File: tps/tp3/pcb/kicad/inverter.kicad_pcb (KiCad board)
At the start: 2 copper layers, 28 parts, among them Q1 IRF820, Q2 IRF820, Q3 IRF820, Q4 IRF820, Q5 IRF820, Q6 IRF820, U1 IR2110-A, U2 ESP32-DEVKIT-V1, U3 IR2110-B, U4 IR2110-C

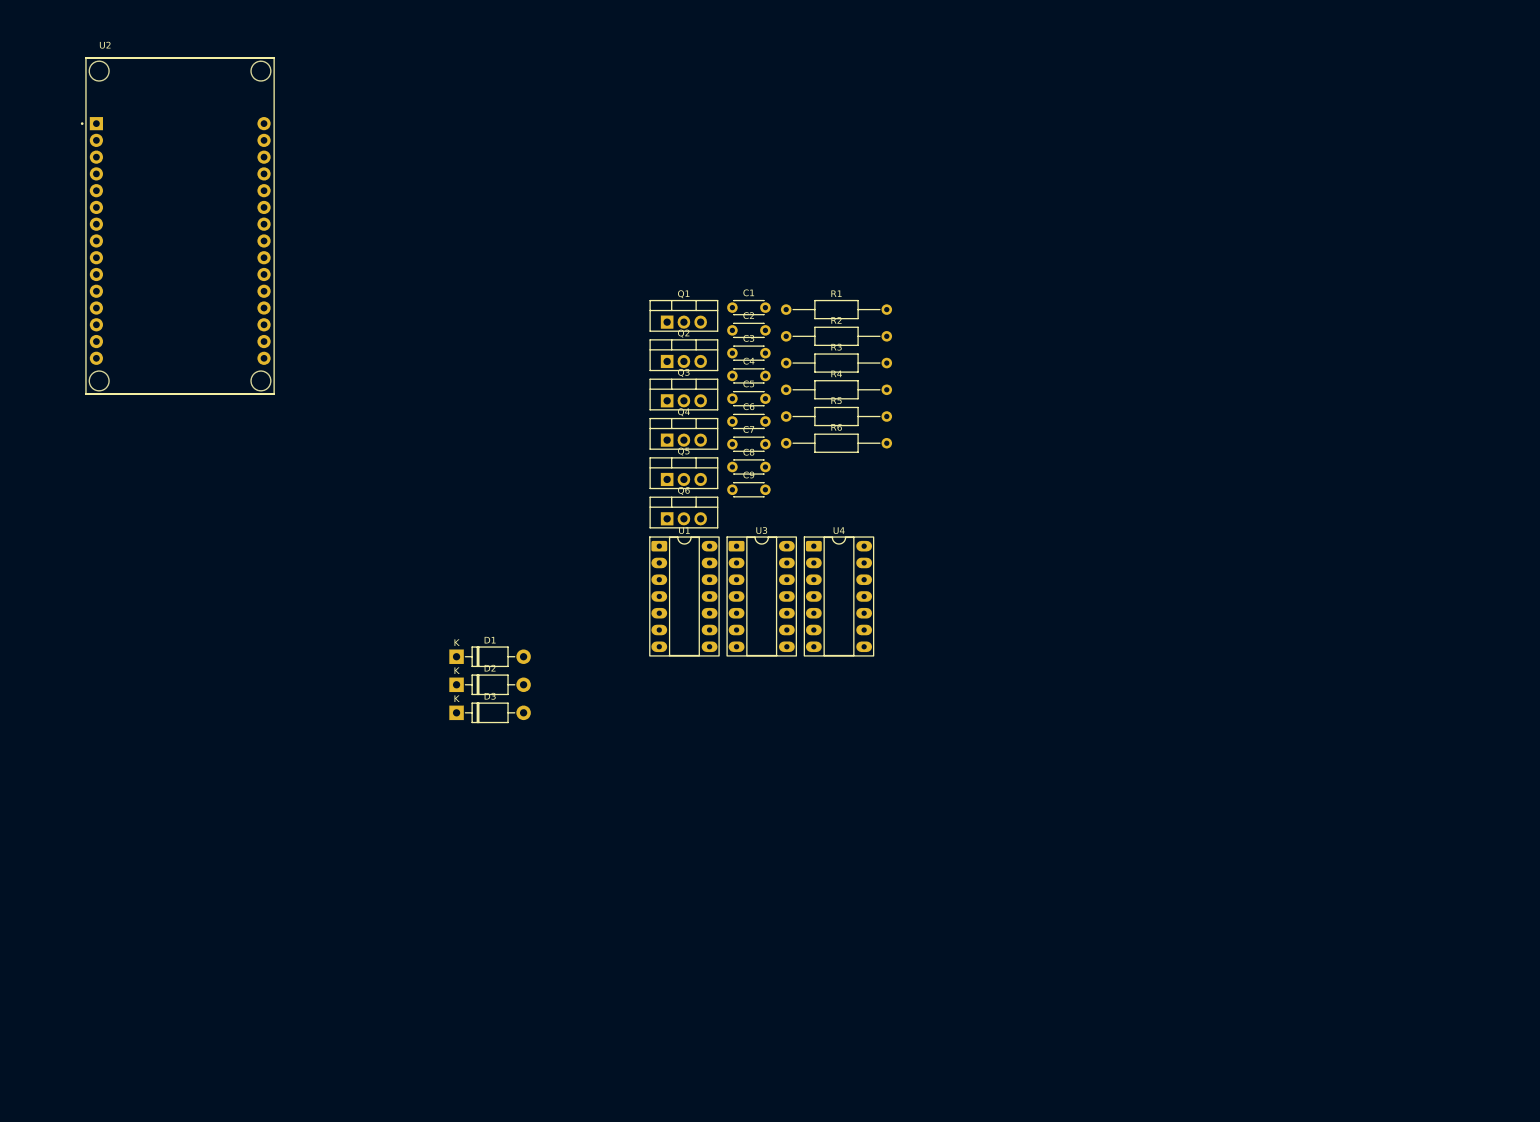
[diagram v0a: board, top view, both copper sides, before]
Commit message: fix inverter sch after feedback and real component sizes, start PCB routing
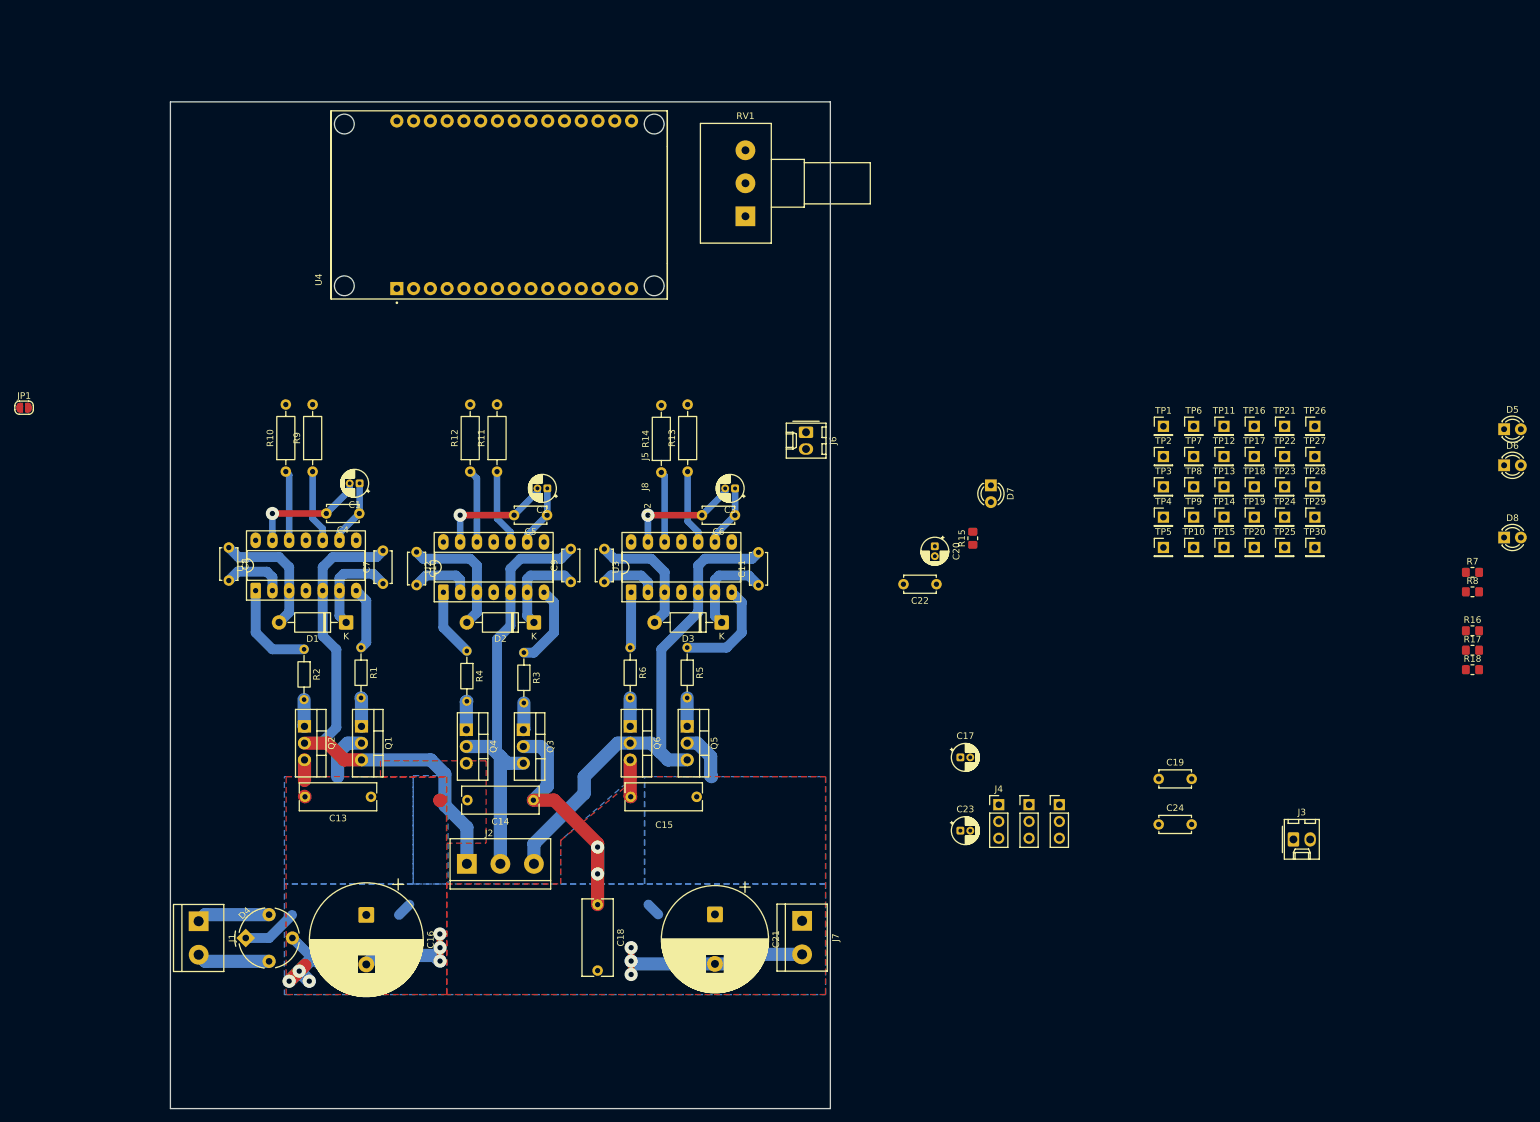
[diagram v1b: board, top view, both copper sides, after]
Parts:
- added C10: 1u-50V, Capacitor_THT:C_Disc_D4.7mm_W2.5mm_P5.00mm, F.Cu at (93.5, 87.4)
- added C11: 1u-50V, Capacitor_THT:C_Disc_D4.7mm_W2.5mm_P5.00mm, F.Cu at (145.3, 92.4)
- added C12: 1u-50V, Capacitor_THT:C_Disc_D4.7mm_W2.5mm_P5.00mm, F.Cu at (121.9, 86.9)
- added C13: 22n-400V, Capacitor_THT:C_Rect_L11.5mm_W4.0mm_P10.00mm_MKT, F.Cu at (86.6, 124.5)
- added C14: 22n-400V, Capacitor_THT:C_Rect_L11.5mm_W4.0mm_P10.00mm_MKT, F.Cu at (111.2, 125.0)
- added C15: 22n-400V, Capacitor_THT:C_Rect_L11.5mm_W4.0mm_P10.00mm_MKT, F.Cu at (135.9, 124.5)
- added C16: 100u-450V, Capacitor_THT:CP_Radial_D17.0mm_P7.50mm, F.Cu at (85.9, 142.4)
- added C17: 10u-25V, Capacitor_THT:CP_Radial_D4.0mm_P1.50mm, F.Cu at (175.9, 118.5)
- added C18: 10n-400V, Capacitor_THT:C_Rect_L11.5mm_W4.5mm_P10.00mm_MKT, F.Cu at (120.9, 140.8)
- added C19: 1u-50V, Capacitor_THT:C_Disc_D4.7mm_W2.5mm_P5.00mm, F.Cu at (205.9, 121.8)
- added C20: 10u-25V, Capacitor_THT:CP_Radial_D4.0mm_P1.50mm, F.Cu at (172.0, 86.5)
- added C21: 47u-450V, Capacitor_THT:CP_Radial_D16.0mm_P7.50mm, F.Cu at (138.7, 142.3)
- added C22: 1u-50V, Capacitor_THT:C_Disc_D4.7mm_W2.5mm_P5.00mm, F.Cu at (172.2, 92.2)
- added C23: 10u-25V, Capacitor_THT:CP_Radial_D4.0mm_P1.50mm, F.Cu at (175.9, 129.6)
- added C24: 1u-50V, Capacitor_THT:C_Disc_D4.7mm_W2.5mm_P5.00mm, F.Cu at (205.9, 128.7)
- added D4: W10M, Diode_THT:Diode_Bridge_Round_D9.0mm, F.Cu at (67.6, 145.9)
- added D5: Red, LED_THT:LED_D3.0mm, F.Cu at (258.3, 68.8)
- added D6: Red, LED_THT:LED_D3.0mm, F.Cu at (258.3, 74.2)
- added D7: Red, LED_THT:LED_D3.0mm, F.Cu at (180.5, 77.3)
- added D8: Red, LED_THT:LED_D3.0mm, F.Cu at (258.3, 85.2)
- added J1: 220Vac In, TerminalBlock:TerminalBlock_bornier-2_P5.08mm, F.Cu at (60.5, 143.3)
- added J2: Motor, TerminalBlock:TerminalBlock_bornier-3_P5.08mm, F.Cu at (101.1, 134.6)
- added J3: 5Vext In, Connector_Molex:Molex_KK-254_AE-6410-02A_1x02_P2.54mm_Vertical, F.Cu at (226.3, 130.9)
- added J4: Conn_01x03_Pin, Connector_PinHeader_2.54mm:PinHeader_1x03_P2.54mm_Vertical, F.Cu at (181.7, 125.7)
- added J5: Conn_01x03_Pin, Connector_PinHeader_2.54mm:PinHeader_1x03_P2.54mm_Vertical, F.Cu at (186.3, 125.7)
- added J6: 15Vext In, Connector_Molex:Molex_KK-254_AE-6410-02A_1x02_P2.54mm_Vertical, F.Cu at (152.5, 69.2)
- added J7: Vd out, TerminalBlock:TerminalBlock_bornier-2_P5.08mm, F.Cu at (151.9, 143.3)
- added J8: Conn_01x03_Pin, Connector_PinHeader_2.54mm:PinHeader_1x03_P2.54mm_Vertical, F.Cu at (190.9, 125.7)
- added JP1: Jumper_2_Bridged, Jumper:SolderJumper-2_P1.3mm_Open_RoundedPad1.0x1.5mm, F.Cu at (34.0, 65.5)
- added R10: 10, Resistor_THT:R_Axial_DIN0207_L6.3mm_D2.5mm_P10.16mm_Horizontal, F.Cu at (73.7, 75.2)
- added R11: 10, Resistor_THT:R_Axial_DIN0207_L6.3mm_D2.5mm_P10.16mm_Horizontal, F.Cu at (105.7, 75.2)
- added R12: 10, Resistor_THT:R_Axial_DIN0207_L6.3mm_D2.5mm_P10.16mm_Horizontal, F.Cu at (101.6, 75.2)
- added R13: 10, Resistor_THT:R_Axial_DIN0207_L6.3mm_D2.5mm_P10.16mm_Horizontal, F.Cu at (134.5, 75.2)
- added R14: 10, Resistor_THT:R_Axial_DIN0207_L6.3mm_D2.5mm_P10.16mm_Horizontal, F.Cu at (130.6, 75.3)
- added R15: 2.7k, Resistor_SMD:R_0805_2012Metric_Pad1.20x1.40mm_HandSolder, F.Cu at (177.8, 85.3)
- added R16: 150k, Resistor_SMD:R_0805_2012Metric_Pad1.20x1.40mm_HandSolder, F.Cu at (253.5, 99.3)
- added R17: 150k, Resistor_SMD:R_0805_2012Metric_Pad1.20x1.40mm_HandSolder, F.Cu at (253.5, 102.2)
- added R18: 150k, Resistor_SMD:R_0805_2012Metric_Pad1.20x1.40mm_HandSolder, F.Cu at (253.5, 105.2)
- added R7: 560, Resistor_SMD:R_0805_2012Metric_Pad1.20x1.40mm_HandSolder, F.Cu at (253.5, 90.5)
- added R8: 220, Resistor_SMD:R_0805_2012Metric_Pad1.20x1.40mm_HandSolder, F.Cu at (253.5, 93.4)
- added R9: 10, Resistor_THT:R_Axial_DIN0207_L6.3mm_D2.5mm_P10.16mm_Horizontal, F.Cu at (77.7, 75.2)
- added RV1: 10k, Potentiometer_THT:Potentiometer_Alps_RK163_Single_Horizontal, F.Cu at (143.3, 36.5)
- added TP1: TestPoint, Connector_PinHeader_2.54mm:PinHeader_1x01_P2.54mm_Vertical, F.Cu at (206.6, 68.3)
- added TP10: TestPoint, Connector_PinHeader_2.54mm:PinHeader_1x01_P2.54mm_Vertical, F.Cu at (211.2, 86.7)
- added TP11: TestPoint, Connector_PinHeader_2.54mm:PinHeader_1x01_P2.54mm_Vertical, F.Cu at (215.8, 68.3)
- added TP12: TestPoint, Connector_PinHeader_2.54mm:PinHeader_1x01_P2.54mm_Vertical, F.Cu at (215.8, 72.9)
- added TP13: TestPoint, Connector_PinHeader_2.54mm:PinHeader_1x01_P2.54mm_Vertical, F.Cu at (215.8, 77.5)
- added TP14: TestPoint, Connector_PinHeader_2.54mm:PinHeader_1x01_P2.54mm_Vertical, F.Cu at (215.8, 82.1)
- added TP15: TestPoint, Connector_PinHeader_2.54mm:PinHeader_1x01_P2.54mm_Vertical, F.Cu at (215.8, 86.7)
- added TP16: TestPoint, Connector_PinHeader_2.54mm:PinHeader_1x01_P2.54mm_Vertical, F.Cu at (220.4, 68.3)
- added TP17: TestPoint, Connector_PinHeader_2.54mm:PinHeader_1x01_P2.54mm_Vertical, F.Cu at (220.4, 72.9)
- added TP18: TestPoint, Connector_PinHeader_2.54mm:PinHeader_1x01_P2.54mm_Vertical, F.Cu at (220.4, 77.5)
- added TP19: TestPoint, Connector_PinHeader_2.54mm:PinHeader_1x01_P2.54mm_Vertical, F.Cu at (220.4, 82.1)
- added TP2: TestPoint, Connector_PinHeader_2.54mm:PinHeader_1x01_P2.54mm_Vertical, F.Cu at (206.6, 72.9)
- added TP20: TestPoint, Connector_PinHeader_2.54mm:PinHeader_1x01_P2.54mm_Vertical, F.Cu at (220.4, 86.7)
- added TP21: TestPoint, Connector_PinHeader_2.54mm:PinHeader_1x01_P2.54mm_Vertical, F.Cu at (225.0, 68.3)
- added TP22: TestPoint, Connector_PinHeader_2.54mm:PinHeader_1x01_P2.54mm_Vertical, F.Cu at (225.0, 72.9)
- added TP23: TestPoint, Connector_PinHeader_2.54mm:PinHeader_1x01_P2.54mm_Vertical, F.Cu at (225.0, 77.5)
- added TP24: TestPoint, Connector_PinHeader_2.54mm:PinHeader_1x01_P2.54mm_Vertical, F.Cu at (225.0, 82.1)
- added TP25: TestPoint, Connector_PinHeader_2.54mm:PinHeader_1x01_P2.54mm_Vertical, F.Cu at (225.0, 86.7)
- added TP26: TestPoint, Connector_PinHeader_2.54mm:PinHeader_1x01_P2.54mm_Vertical, F.Cu at (229.6, 68.3)
- added TP27: TestPoint, Connector_PinHeader_2.54mm:PinHeader_1x01_P2.54mm_Vertical, F.Cu at (229.6, 72.9)
- added TP28: TestPoint, Connector_PinHeader_2.54mm:PinHeader_1x01_P2.54mm_Vertical, F.Cu at (229.6, 77.5)
- added TP29: TestPoint, Connector_PinHeader_2.54mm:PinHeader_1x01_P2.54mm_Vertical, F.Cu at (229.6, 82.1)
- added TP3: TestPoint, Connector_PinHeader_2.54mm:PinHeader_1x01_P2.54mm_Vertical, F.Cu at (206.6, 77.5)
- added TP30: TestPoint, Connector_PinHeader_2.54mm:PinHeader_1x01_P2.54mm_Vertical, F.Cu at (229.6, 86.7)
- added TP4: TestPoint, Connector_PinHeader_2.54mm:PinHeader_1x01_P2.54mm_Vertical, F.Cu at (206.6, 82.1)
- added TP5: TestPoint, Connector_PinHeader_2.54mm:PinHeader_1x01_P2.54mm_Vertical, F.Cu at (206.6, 86.7)
- added TP6: TestPoint, Connector_PinHeader_2.54mm:PinHeader_1x01_P2.54mm_Vertical, F.Cu at (211.2, 68.3)
- added TP7: TestPoint, Connector_PinHeader_2.54mm:PinHeader_1x01_P2.54mm_Vertical, F.Cu at (211.2, 72.9)
- added TP8: TestPoint, Connector_PinHeader_2.54mm:PinHeader_1x01_P2.54mm_Vertical, F.Cu at (211.2, 77.5)
- added TP9: TestPoint, Connector_PinHeader_2.54mm:PinHeader_1x01_P2.54mm_Vertical, F.Cu at (211.2, 82.1)
- C1, C3: value 1u -> 10u-25V; footprint Capacitor_THT:C_Disc_D4.3mm_W1.9mm_P5.00mm -> Capacitor_THT:CP_Radial_D4.0mm_P1.50mm
- C2: value 10u -> 10u-25V; footprint Capacitor_THT:C_Disc_D4.3mm_W1.9mm_P5.00mm -> Capacitor_THT:CP_Radial_D4.0mm_P1.50mm
- C4, C5, C7, C8: value 1u -> 1u-50V; footprint Capacitor_THT:C_Disc_D4.3mm_W1.9mm_P5.00mm -> Capacitor_THT:C_Disc_D4.7mm_W2.5mm_P5.00mm
- C6, C9: value 10u -> 1u-50V; footprint Capacitor_THT:C_Disc_D4.3mm_W1.9mm_P5.00mm -> Capacitor_THT:C_Disc_D4.7mm_W2.5mm_P5.00mm
- D1, D2, D3: value 1N5819 -> FR104
- R1, R2, R3, R4, R5, R6: footprint Resistor_THT:R_Axial_DIN0207_L6.3mm_D2.5mm_P15.24mm_Horizontal -> Resistor_THT:R_Axial_DIN0204_L3.6mm_D1.6mm_P7.62mm_Horizontal
- U2: value ESP32-DEVKIT-V1 -> IR2110-B; footprint esp32devkitv1:MODULE_ESP32_DEVKIT_V1 -> Package_DIP:DIP-14_W7.62mm_Socket_LongPads
- U3: value IR2110-B -> IR2110-C
- U4: value IR2110-C -> ESP32-DEVKIT-V1; footprint Package_DIP:DIP-14_W7.62mm_Socket_LongPads -> esp32devkitv1:MODULE_ESP32_DEVKIT_V1
- moved R2 87.1 mm to (76.4, 102.1), turned to -90 degrees
- moved R1 82.3 mm to (85.1, 101.9), turned to -90 degrees
- moved Q2 78.0 mm to (76.5, 113.8), turned to -90 degrees
- moved C8 77.3 mm to (65.0, 86.7), turned to -90 degrees
- moved Q1 76.8 mm to (85.1, 113.8), turned to -90 degrees
- moved U4 70.4 mm to (106.0, 34.8), turned to 90 degrees
- moved U2 68.3 mm to (97.5, 93.5), turned to 90 degrees
- moved R4 62.5 mm to (101.1, 102.4), turned to -90 degrees
- moved C1 62.5 mm to (84.8, 77.0), turned to 180 degrees
- moved U1 61.5 mm to (69.1, 93.2), turned to 90 degrees
- moved C4 60.3 mm to (84.8, 81.5), turned to 180 degrees
- moved R3 59.2 mm to (109.7, 102.6), turned to -90 degrees
- moved C7 57.0 mm to (88.4, 92.2), turned to 90 degrees
- moved Q3 54.4 mm to (109.6, 114.3), turned to -90 degrees
- moved Q4 53.4 mm to (101.0, 114.3), turned to -90 degrees
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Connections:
- C1 pad 1: Net-(D1-K) -> VDD
- C1 pad 2: /OUT_A -> VSS
- C2 pad 1: VIC -> VDD
- C2 pad 2: COM -> VSS
- C5 pad 1: Net-(D2-K) -> VDD
- C5 pad 2: /OUT_B -> VSS
- C6 pad 1: VIC -> VDD
- C6 pad 2: COM -> VSS
- C7 pad 1: VDD -> Net-(D1-K)
- C7 pad 2: VSS -> /OUT_A
- C8 pad 1: Net-(D3-K) -> VDRV
- C8 pad 2: /OUT_C -> COM
- C9 pad 1: VIC -> Net-(D2-K)
- C9 pad 2: COM -> /OUT_B
- D1 pad 2: VIC -> VDRV
- D2 pad 2: VIC -> VDRV
- D3 pad 2: VIC -> VDRV
- R3 pad 1: Net-(U3-HO) -> Net-(U2-HO)
- R4 pad 1: Net-(U3-LO) -> Net-(U2-LO)
- R5 pad 1: Net-(U4-HO) -> Net-(U3-HO)
- R6 pad 1: Net-(U4-LO) -> Net-(U3-LO)
- U1 pad 3: VIC -> VDRV
- U2 pad 1: unconnected-(U2-3V3-Pad1) -> Net-(U2-LO)
- U2 pad 10: unconnected-(U2-D19-Pad10) -> /HIN_B
- U2 pad 12: unconnected-(U2-RX0-Pad12) -> /LIN_B
- U2 pad 13: unconnected-(U2-TX0-Pad13) -> VSS
- U2 pad 2: Net-(U2-GND-Pad2) -> COM
- U2 pad 3: unconnected-(U2-D15-Pad3) -> VDRV
- U2 pad 5: unconnected-(U2-D4-Pad5) -> /OUT_B
- U2 pad 6: unconnected-(U2-RX2-Pad6) -> Net-(D2-K)
- U2 pad 7: unconnected-(U2-TX2-Pad7) -> Net-(U2-HO)
- U2 pad 9: unconnected-(U2-D18-Pad9) -> VDD
- U3 pad 10: /HIN_B -> /HIN_C
- U3 pad 12: /LIN_B -> /LIN_C
- U3 pad 3: VIC -> VDRV
- U3 pad 5: /OUT_B -> /OUT_C
- U3 pad 6: Net-(D2-K) -> Net-(D3-K)
- U4 pad 1: Net-(U4-LO) -> VDD
- U4 pad 10: /HIN_C -> Net-(U4-D19)
- U4 pad 11: unconnected-(U4-SD-Pad11) -> Net-(U4-D21)
- U4 pad 12: /LIN_C -> unconnected-(U4-RX0-Pad12)
- U4 pad 13: VSS -> unconnected-(U4-TX0-Pad13)
- U4 pad 2: COM -> VSS
- U4 pad 3: VIC -> Net-(U4-D15)
- U4 pad 5: /OUT_C -> unconnected-(U4-D4-Pad5)
- U4 pad 6: Net-(D3-K) -> unconnected-(U4-RX2-Pad6)
- U4 pad 7: Net-(U4-HO) -> unconnected-(U4-TX2-Pad7)
- U4 pad 9: VDD -> Net-(U4-D18)
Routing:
- net COM: track 0.00 -> 100.2 mm, vias 0 -> 9
- net /OUT_A: track 0.00 -> 79.4 mm
- net /OUT_C: track 0.00 -> 75.7 mm
- net VD: track 0.00 -> 65.9 mm, vias 0 -> 2
- net /OUT_B: track 0.00 -> 65.8 mm
- net VDRV: track 0.00 -> 57.5 mm
- net VSS: track 0.00 -> 53.8 mm, vias 0 -> 3
- net VDD: track 0.00 -> 28.8 mm
- net Net-(U3-HO): track 0.00 -> 15.9 mm
- net Net-(U1-LO): track 0.00 -> 14.7 mm
- net Net-(D1-K): track 0.00 -> 14.6 mm
- net Net-(D3-K): track 0.00 -> 14.4 mm
- net Net-(D2-K): track 0.00 -> 14.2 mm
- net Net-(U2-HO): track 0.00 -> 12.6 mm
- net /HIN_B: track 0.00 -> 11.5 mm
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- added copper zone on F.Cu, net COM
- added copper zone on B.Cu, net VD
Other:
- board outline added: 100 x 152.5 mm

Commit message: add more 15V decoupling caps, update exported sch, add potentiometer 3D model, some routing progress
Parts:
- added C25: 10u-25V, Capacitor_THT:CP_Radial_D4.0mm_P1.50mm, F.Cu at (93.5, 82.0)
- added C26: 10u-25V, Capacitor_THT:CP_Radial_D4.0mm_P1.50mm, F.Cu at (65.0, 81.8)
- added C27: 10u-25V, Capacitor_THT:CP_Radial_D4.0mm_P1.50mm, F.Cu at (122.0, 82.0)
- R15: moved to B.Cu
- moved D7 28.8 mm to (152.0, 73.0), turned to 180 degrees
- moved R15 25.1 mm to (154.0, 77.2)
- moved C22 22.5 mm to (151.2, 84.2), turned to -90 degrees
- moved J6 9.09 mm to (151.2, 78.2)
- moved C21 1.43 mm to (137.2, 142.3)
- moved C10 0.13 mm to (93.5, 87.5)
- moved C12 0.12 mm to (122.0, 87.0)
- moved C8 0.06 mm to (65.0, 86.8)
- turned U4 to -90 degrees
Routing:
- net VDRV: track 57.5 -> 208.7 mm
- net COM: track 100.2 -> 153.1 mm
- net VD: track 65.9 -> 55.7 mm, vias 2 -> 3
- net Net-(D7-K): track 0.00 -> 4.62 mm
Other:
- board size 100 x 152.5 mm -> 100 x 150 mm

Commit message: avances pcb
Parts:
- added C28: 10u-25V, Capacitor_THT:CP_Radial_D4.0mm_P1.50mm, F.Cu at (171.0, 44.8)
- added C29: 10u-25V, Capacitor_THT:CP_Radial_D4.0mm_P1.50mm, F.Cu at (171.0, 50.3)
- added C30: 10u-25V, Capacitor_THT:CP_Radial_D4.0mm_P1.50mm, F.Cu at (171.0, 55.9)
- moved C22 47.2 mm to (190.5, 58.0)
- moved D7 47.2 mm to (191.3, 46.8)
- moved J6 47.2 mm to (190.5, 52.0)
- moved R15 47.2 mm to (193.2, 51.0)
- moved C18 31.5 mm to (89.5, 140.8)
- moved R14 23.1 mm to (144.5, 93.7)
- moved R9 22.6 mm to (64.0, 93.1)
- moved C26 21.5 mm to (62.3, 103.1), turned to -135 degrees
- moved C3 21.1 mm to (149.1, 97.5), turned to 135 degrees
- moved C8 19.9 mm to (65.9, 106.7), turned to -45 degrees
- moved D4 19.8 mm to (70.4, 126.3), turned to -45 degrees
- moved C6 19.1 mm to (146.2, 100.4), turned to 135 degrees
- moved C11 18.4 mm to (141.2, 110.4), turned to 45 degrees
- moved R10 16.7 mm to (68.0, 90.9)
- moved R13 16.2 mm to (140.2, 90.3)
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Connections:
- R10 pad 1: /LIN_A -> /HIN_A
- R10 pad 2: Net-(U4-D14) -> Net-(U4-D2)
- R11 pad 1: /HIN_B -> /LIN_B
- R11 pad 2: Net-(U4-D15) -> Net-(U4-D4)
- R12 pad 1: /LIN_B -> /HIN_B
- R12 pad 2: Net-(U4-D18) -> Net-(U4-RX2)
- R13 pad 1: /HIN_C -> /LIN_C
- R13 pad 2: Net-(U4-D19) -> Net-(U4-TX2)
- R14 pad 1: /LIN_C -> /HIN_C
- R14 pad 2: Net-(U4-D21) -> Net-(U4-D5)
- R9 pad 1: /HIN_A -> /LIN_A
- R9 pad 2: Net-(U4-D13) -> Net-(U4-D15)
- RV1 pad 2: Net-(U4-D27) -> Net-(U4-D34)
- TP29 pad 1: Net-(U4-D27) -> Net-(U4-D34)
- U4 pad 10: Net-(U4-D19) -> unconnected-(U4-D19-Pad10)
- U4 pad 11: Net-(U4-D21) -> unconnected-(U4-D21-Pad11)
- U4 pad 19: Net-(J8-Pin_1) -> Net-(U4-D34)
- U4 pad 20: Net-(J8-Pin_2) -> unconnected-(U4-D35-Pad20)
- U4 pad 22: Net-(J8-Pin_3) -> unconnected-(U4-D33-Pad22)
- U4 pad 23: unconnected-(U4-D25-Pad23) -> Net-(J8-Pin_3)
- U4 pad 24: unconnected-(U4-D26-Pad24) -> Net-(J8-Pin_2)
- U4 pad 25: Net-(U4-D27) -> Net-(J8-Pin_1)
- U4 pad 26: Net-(U4-D14) -> unconnected-(U4-D14-Pad26)
- U4 pad 28: Net-(U4-D13) -> unconnected-(U4-D13-Pad28)
- U4 pad 4: unconnected-(U4-D2-Pad4) -> Net-(U4-D2)
- U4 pad 5: unconnected-(U4-D4-Pad5) -> Net-(U4-D4)
- U4 pad 6: unconnected-(U4-RX2-Pad6) -> Net-(U4-RX2)
- U4 pad 7: unconnected-(U4-TX2-Pad7) -> Net-(U4-TX2)
- U4 pad 8: unconnected-(U4-D5-Pad8) -> Net-(U4-D5)
- U4 pad 9: Net-(U4-D18) -> unconnected-(U4-D18-Pad9)
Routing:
- net VD: track 55.7 -> 179.2 mm, vias 3 -> 2
- net VDRV: track 208.7 -> 89.4 mm
- net COM: track 153.1 -> 134.2 mm, vias 9 -> 0
- net /OUT_A: track 79.4 -> 64.2 mm
- net /OUT_C: track 75.7 -> 64.0 mm
- net /HIN_B: track 11.5 -> 0.00 mm
- net /HIN_C: track 11.3 -> 0.00 mm
- net /LIN_B: track 11.1 -> 0.00 mm
- net /HIN_A: track 11.0 -> 0.00 mm
- net /LIN_C: track 10.8 -> 0.00 mm
- net /LIN_A: track 10.6 -> 0.00 mm
- net Net-(U3-HO): track 15.9 -> 5.76 mm
- net Net-(U1-LO): track 14.7 -> 6.35 mm
- net NEUT: track 11.1 -> 7.34 mm
- net LINE: track 11.1 -> 14.5 mm
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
